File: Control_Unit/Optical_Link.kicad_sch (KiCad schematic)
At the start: 16 parts, among them J2 Conn_01x03_Pin, J3 Conn_01x03_Pin, J4 Conn_01x04_Pin, J5 Conn_01x05_Pin, Q1 2N3904, Q2 IRF9540N, Q3 2N3904

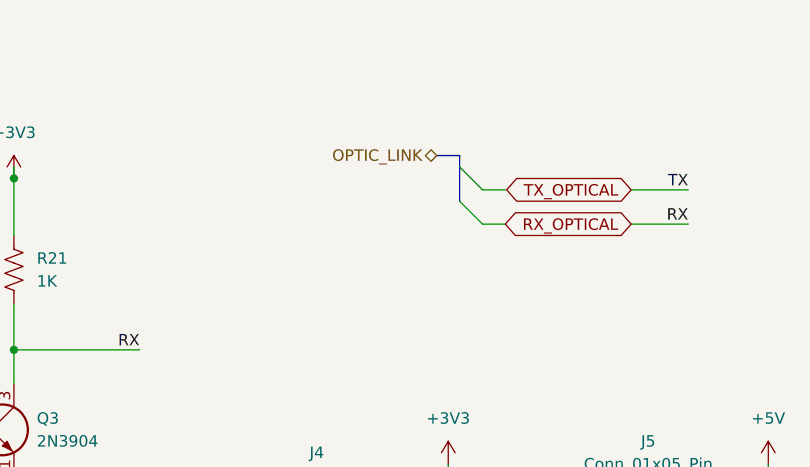
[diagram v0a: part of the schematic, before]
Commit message: Control Unit Schematics and PCB.
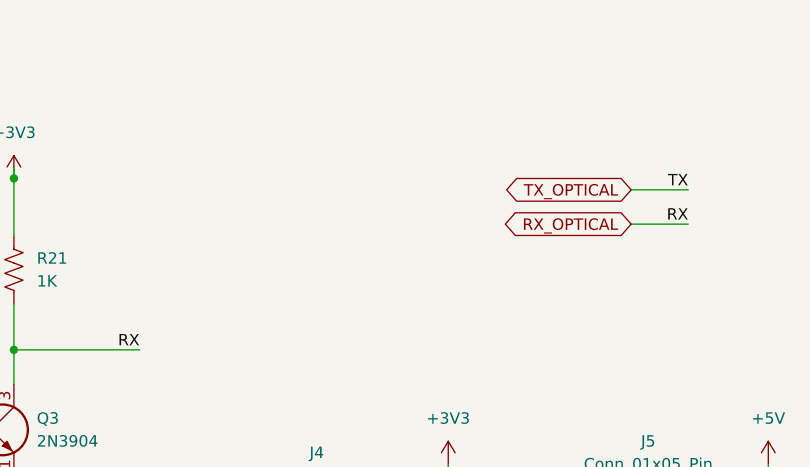
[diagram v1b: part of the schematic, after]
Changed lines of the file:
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@@
 		(color 0 0 0 0)
 	)
-	(bus_entry
-		(at 224.79 73.66)
-		(size 2.54 2.54)
-		(stroke
-			(width 0)
-			(type default)
-		)
-	)
-	(bus_entry
-		(at 224.79 69.85)
-		(size 2.54 2.54)
-		(stroke
-			(width 0)
-			(type default)
-		)
-	)
 	(wire
 		(pts
@@
 		)
 	)
-	(bus
-		(pts
-			(xy 224.79 69.85) (xy 224.79 68.58)
-		)
-		(stroke
-			(width 0)
-			(type default)
-		)
-	)
 	(wire
 		(pts
@@
 		)
 	)
-	(bus
-		(pts
-			(xy 224.79 68.58) (xy 222.25 68.58)
-		)
-		(stroke
-			(width 0)
-			(type default)
-		)
-	)
 	(wire
 		(pts
@@
 	(wire
 		(pts
-			(xy 227.33 72.39) (xy 229.87 72.39)
-		)
-		(stroke
-			(width 0)
-			(type default)
-		)
-	)
-	(wire
-		(pts
 			(xy 175.26 90.17) (xy 189.23 90.17)
 		)
@@
 		)
 	)
-	(bus
-		(pts
-			(xy 224.79 73.66) (xy 224.79 69.85)
-		)
-		(stroke
-			(width 0)
-			(type default)
-		)
-	)
 	(wire
 		(pts
@@
 		(pts
 			(xy 213.36 109.22) (xy 223.52 109.22)
-		)
-		(stroke
-			(width 0)
-			(type default)
-		)
-	)
-	(wire
-		(pts
-			(xy 227.33 76.2) (xy 229.87 76.2)
 		)
 		(stroke
@@
 		)
 	)
-	(hierarchical_label "OPTIC_LINK"
-		(shape bidirectional)
-		(at 222.25 68.58 180)
-		(effects
-			(font
-				(size 1.27 1.27)
-			)
-			(justify right)
-		)
-	)

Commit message: Final Control Unit Schematic Rev 1.
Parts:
- R14, R17: value 15R -> 15R/ 1%/ 0W125
- R15: value 100R -> 100R/ 1%/ 0W125
- R16: value 10K -> 10K/ 1%/ 0W6
- R18, R21: value 1K -> 1K/ 1%/ 0W6
- R19: value 1K -> 1K/ 1%/ 0W61K
- R20: value 100 -> 100R/ 1%/ 0W125
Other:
- note added: "Optical Link"
- title: (none) -> ENGG3800 Team 03: Loggy
- moved on the sheet: J2, J3, J4, J5, Q1, Q2, Q3, R14, R15, R16, R17, R18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
